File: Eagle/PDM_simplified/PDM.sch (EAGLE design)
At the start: 29 parts, among them U1 MIC29150/29300/29500VERTICAL

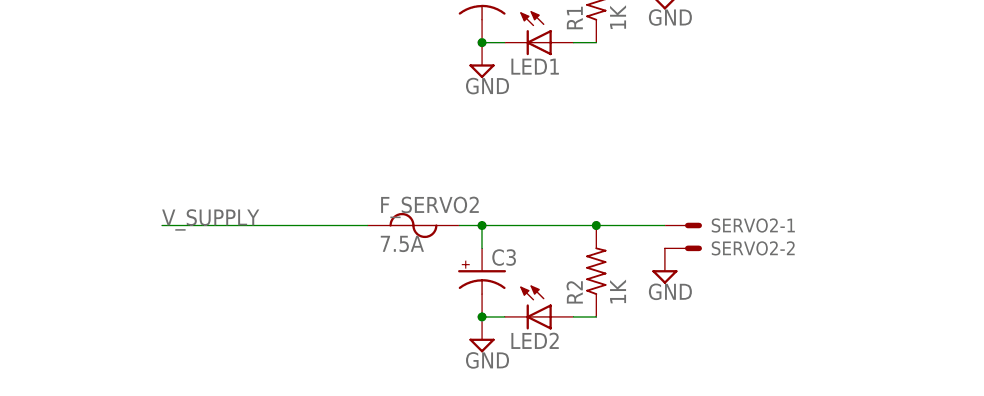
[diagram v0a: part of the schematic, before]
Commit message: Updated PDM
1 Power Supply channel
1 servo channel
1 camera channel
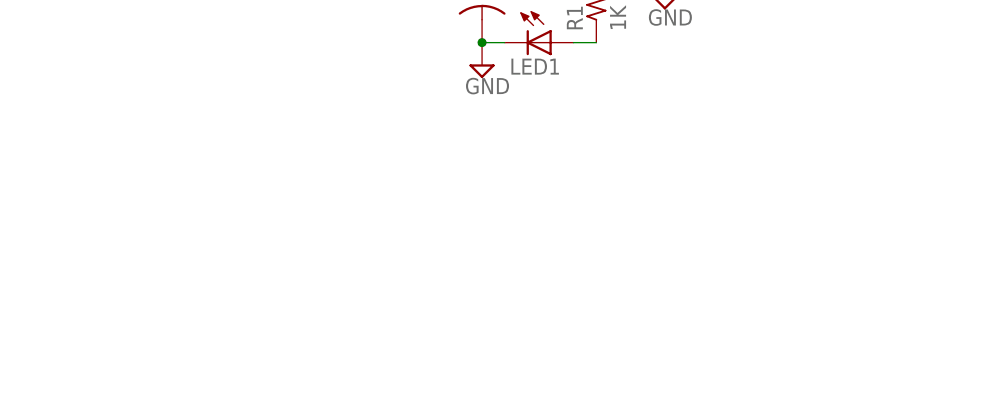
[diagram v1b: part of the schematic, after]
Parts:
- removed C3: (no value), rcl:CPOL-USTT5D11
- removed F_SERVO2: 7.5A, MRSDTeamB:FUSE-ATO
- removed LED2: (no value), led:LEDSML1206
- removed R2: 1K, rcl:R-US_R1206
- removed SERVO2: 5566-2, con-molex:5566-2
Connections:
- removed net N$1: C3.+, F_SERVO2.2, R2.2, SERVO2-1.S
- removed net N$8: LED2.A, R2.1
- net GND: no longer C3.-, LED2.C, SERVO2-2.S
- net V_SUPPLY: no longer F_SERVO2.1
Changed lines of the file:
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@@
 <part name="SUPPLY1" library="supply2" deviceset="GND" device=""/>
 <part name="SUPPLY3" library="supply2" deviceset="GND" device=""/>
-<part name="SUPPLY5" library="supply2" deviceset="GND" device=""/>
 <part name="SUPPLY6" library="supply2" deviceset="GND" device=""/>
 <part name="SUPPLY7" library="supply2" deviceset="GND" device=""/>
 <part name="SUPPLY11" library="supply2" deviceset="GND" device=""/>
 <part name="SUPPLY12" library="supply2" deviceset="GND" device=""/>
-<part name="SUPPLY14" library="supply2" deviceset="GND" device=""/>
-<part name="LED2" library="led" deviceset="LED" device="SML1206"/>
 <part name="LED3" library="led" deviceset="LED" device="SML1206"/>
 <part name="LED4" library="led" deviceset="LED" device="SML1206"/>
@@
 <part name="BAT_MON" library="con-samtec" deviceset="TSW-101-02-S-S" device="" value=""/>
 <part name="R1" library="rcl" deviceset="R-US_" device="R1206" value="1K"/>
-<part name="R2" library="rcl" deviceset="R-US_" device="R1206" value="1K"/>
 <part name="R3" library="rcl" deviceset="R-US_" device="R1206" value="1K"/>
 <part name="R4" library="rcl" deviceset="R-US_" device="R1206" value="1K"/>
@@
 <part name="D2" library="diode" deviceset="ZENER-DIODE" device="SMB" value="3.3V"/>
 <part name="DUE" library="con-molex" deviceset="5566-2" device="" value=""/>
-<part name="SERVO2" library="con-molex" deviceset="5566-2" device="" value=""/>
 <part name="F_BATT" library="MRSDTeamB" deviceset="FUSE-" device="ATO" value="15A"/>
 <part name="F_DUE" library="MRSDTeamB" deviceset="FUSE-" device="ATO" value="2A"/>
 <part name="F_SERVO1" library="MRSDTeamB" deviceset="FUSE-" device="ATO" value="7.5A"/>
-<part name="F_SERVO2" library="MRSDTeamB" deviceset="FUSE-" device="ATO" value="7.5A"/>
 <part name="ACC1" library="con-molex" deviceset="5566-2" device="" value=""/>
 <part name="C2" library="rcl" deviceset="CPOL-US" device="TT5D11"/>
-<part name="C3" library="rcl" deviceset="CPOL-US" device="TT5D11"/>
 <part name="BATT1_W" library="MRSDTeamB" deviceset="CON_XT60-" device="PIGTAIL" value=""/>
 <part name="U1" library="MRSDTeamB" deviceset="MIC29150/29300/29500" device="VERTICAL" value=""/>
@@
 <instance part="SUPPLY1" gate="GND" x="38.1" y="144.78"/>
 <instance part="SUPPLY3" gate="GND" x="256.54" y="167.64"/>
-<instance part="SUPPLY5" gate="GND" x="170.18" y="106.68"/>
 <instance part="SUPPLY6" gate="GND" x="170.18" y="167.64"/>
 <instance part="SUPPLY7" gate="GND" x="294.64" y="175.26"/>
 <instance part="SUPPLY11" gate="GND" x="149.86" y="157.48"/>
 <instance part="SUPPLY12" gate="GND" x="287.02" y="160.02"/>
-<instance part="SUPPLY14" gate="GND" x="149.86" y="99.06"/>
-<instance part="LED2" gate="G$1" x="157.48" y="101.6" rot="R270"/>
 <instance part="LED3" gate="G$1" x="157.48" y="162.56" rot="R270"/>
 <instance part="LED4" gate="G$1" x="287.02" y="167.64"/>
@@
 <instance part="BAT_MON" gate="-1" x="62.23" y="121.92"/>
 <instance part="R1" gate="G$1" x="162.56" y="137.16" rot="R90"/>
-<instance part="R2" gate="G$1" x="162.56" y="106.68" rot="R90"/>
 <instance part="R3" gate="G$1" x="162.56" y="167.64" rot="R90"/>
 <instance part="R4" gate="G$1" x="287.02" y="175.26" rot="R90"/>
@@
 <instance part="DUE" gate="-1" x="172.72" y="172.72"/>
 <instance part="DUE" gate="-2" x="172.72" y="170.18"/>
-<instance part="SERVO2" gate="-1" x="172.72" y="111.76"/>
-<instance part="SERVO2" gate="-2" x="172.72" y="109.22"/>
 <instance part="F_BATT" gate="G$1" x="60.96" y="170.18"/>
 <instance part="F_DUE" gate="G$1" x="142.24" y="172.72"/>
 <instance part="F_SERVO1" gate="G$1" x="142.24" y="142.24"/>
-<instance part="F_SERVO2" gate="G$1" x="142.24" y="111.76"/>
 <instance part="ACC1" gate="-1" x="297.18" y="180.34"/>
 <instance part="ACC1" gate="-2" x="297.18" y="177.8"/>
 <instance part="C2" gate="G$1" x="149.86" y="137.16"/>
-<instance part="C3" gate="G$1" x="149.86" y="106.68"/>
 <instance part="BATT1_W" gate="G$1" x="43.18" y="167.64"/>
 <instance part="U1" gate="G$1" x="256.54" y="177.8"/>
@@
 </segment>
 <segment>
-<pinref part="SUPPLY14" gate="GND" pin="GND"/>
-<pinref part="LED2" gate="G$1" pin="C"/>
-<wire x1="152.4" y1="101.6" x2="149.86" y2="101.6" width="0.1524" layer="91"/>
-<pinref part="C3" gate="G$1" pin="-"/>
-<junction x="149.86" y="101.6"/>
-</segment>
-<segment>
 <pinref part="SERVO1" gate="-2" pin="S"/>
 <pinref part="SUPPLY15" gate="GND" pin="GND"/>
@@
 <pinref part="SUPPLY6" gate="GND" pin="GND"/>
 <pinref part="DUE" gate="-2" pin="S"/>
-</segment>
-<segment>
-<pinref part="SUPPLY5" gate="GND" pin="GND"/>
-<pinref part="SERVO2" gate="-2" pin="S"/>
 </segment>
 <segment>
@@
 <junction x="38.1" y="165.1"/>
 <wire x1="38.1" y1="203.2" x2="38.1" y2="165.1" width="0.1524" layer="91"/>
-</segment>
-</net>
-<net name="N$1" class="0">
-<segment>
-<pinref part="R2" gate="G$1" pin="2"/>
-<pinref part="SERVO2" gate="-1" pin="S"/>
-<wire x1="162.56" y1="111.76" x2="170.18" y2="111.76" width="0.1524" layer="91"/>
-<pinref part="F_SERVO2" gate="G$1" pin="2"/>
-<wire x1="162.56" y1="111.76" x2="149.86" y2="111.76" width="0.1524" layer="91"/>
-<junction x="162.56" y="111.76"/>
-<pinref part="C3" gate="G$1" pin="+"/>
-<wire x1="149.86" y1="111.76" x2="147.32" y2="111.76" width="0.1524" layer="91"/>
-<wire x1="149.86" y1="109.22" x2="149.86" y2="111.76" width="0.1524" layer="91"/>
-<junction x="149.86" y="111.76"/>
 </segment>
 </net>
@@
 </segment>
 </net>
-<net name="N$8" class="0">
-<segment>
-<pinref part="LED2" gate="G$1" pin="A"/>
-<pinref part="R2" gate="G$1" pin="1"/>
-<wire x1="160.02" y1="101.6" x2="162.56" y2="101.6" width="0.1524" layer="91"/>
-</segment>
-</net>
 <net name="N$11" class="0">
 <segment>
@@
 </segment>
 <segment>
-<wire x1="114.3" y1="111.76" x2="137.16" y2="111.76" width="0.1524" layer="91"/>
-<label x="114.3" y="111.76" size="1.778" layer="95"/>
-<pinref part="F_SERVO2" gate="G$1" pin="1"/>
-</segment>
-<segment>

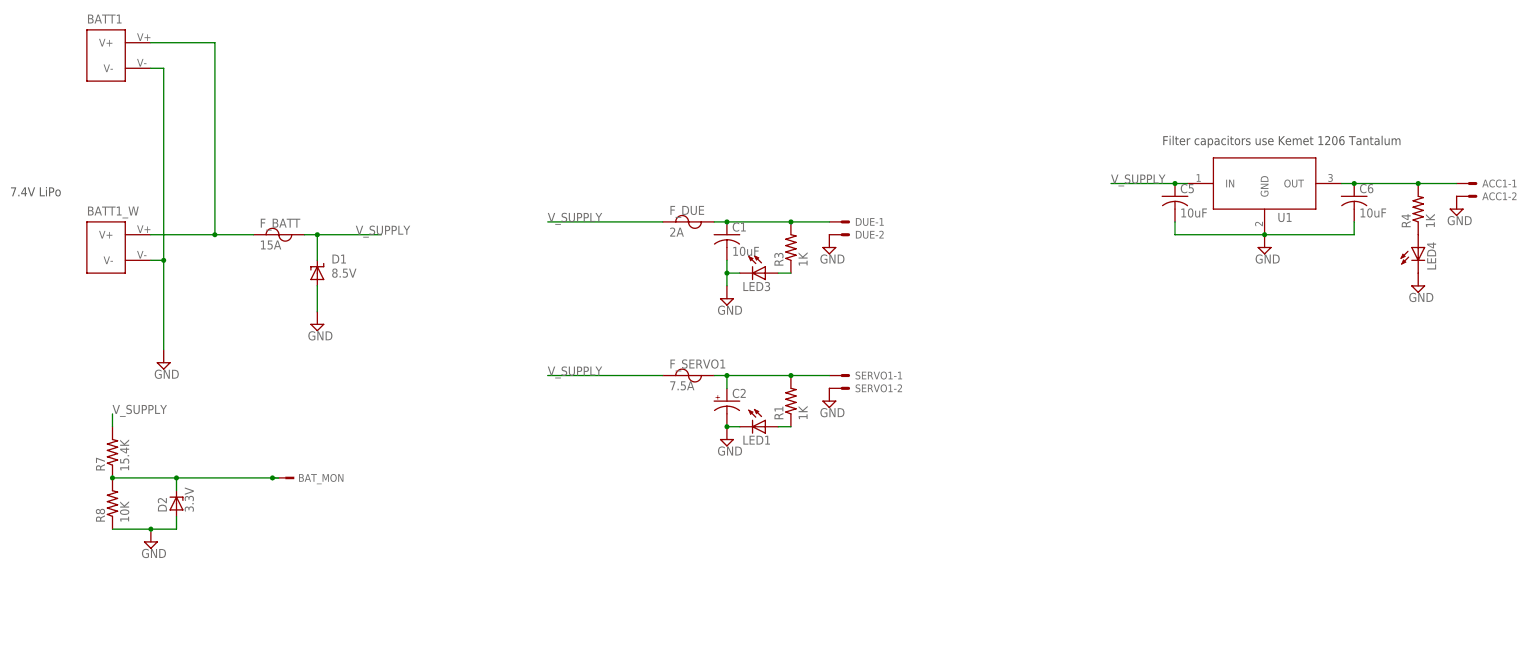
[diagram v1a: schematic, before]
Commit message: Miniaturized PDM
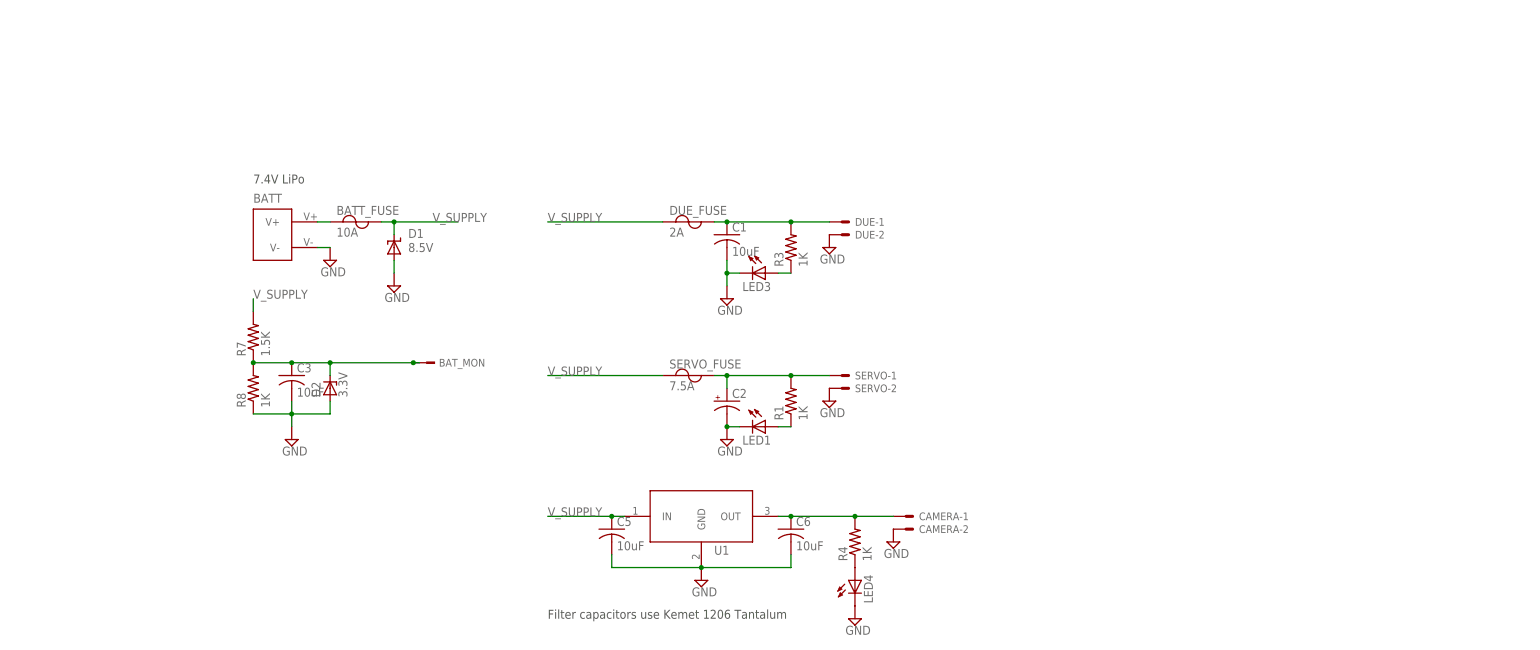
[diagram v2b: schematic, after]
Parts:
- removed ACC1: 5566-2, con-molex:5566-2
- removed BATT1: CON_XT60-PCB_MOUNT, MRSDTeamB:CON_XT60-PCB_MOUNT
- removed BATT1_W: CON_XT60-PIGTAIL, MRSDTeamB:CON_XT60-PIGTAIL
- removed F_BATT: 15A, MRSDTeamB:FUSE-ATO
- removed F_DUE: 2A, MRSDTeamB:FUSE-ATO
- removed F_SERVO1: 7.5A, MRSDTeamB:FUSE-ATO
- added BATT: CON_XT60-, MRSDTeamB:CON_XT60-
- added BATT_FUSE: 10A, MRSDTeamB:FUSE-
- added C3: 10uF, rcl:C-USC1206K
- added CAMERA: 5566-2, con-molex:5566-2
- added DUE_FUSE: 2A, MRSDTeamB:FUSE-
- added SERVO_FUSE: 7.5A, MRSDTeamB:FUSE-
- D2: device diode:ZENER-DIODESMB -> diode:ZENER-DIODESOD80C
- R7: value 15.4K -> 1.5K
- R8: value 10K -> 1K
- renumbered SERVO1 to SERVO
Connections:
- net GND: now also BATT.V-, C3.2, CAMERA-2.S; no longer ACC1-2.S, BATT1.V-, BATT1_W.V-
- net N$15: now also SERVO_FUSE.2; no longer F_SERVO1.2
- net N$18: now also C3.1
- net N$2: now also BATT.V+, BATT_FUSE.1; no longer BATT1.V+, BATT1_W.V+, F_BATT.1
- net N$4: now also DUE_FUSE.2; no longer F_DUE.2
- net N$6: now also CAMERA-1.S; no longer ACC1-1.S
- net V_SUPPLY: now also BATT_FUSE.2, DUE_FUSE.1, SERVO_FUSE.1; no longer F_BATT.2, F_DUE.1, F_SERVO1.1
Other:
- moved on the sheet: BAT_MON, C5, C6, D1, D2, LED4, R4, R7, R8, U1
